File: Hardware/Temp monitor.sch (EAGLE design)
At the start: 41 parts, among them IC1 74LS595D, IC2 74LS595D, IC3 74LS595D, IC4 74LS595D, IC5 74LS595D, J2 TP_8, J3 USB-MICROB, T1 NPN, T2 NPN, T3 NPN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

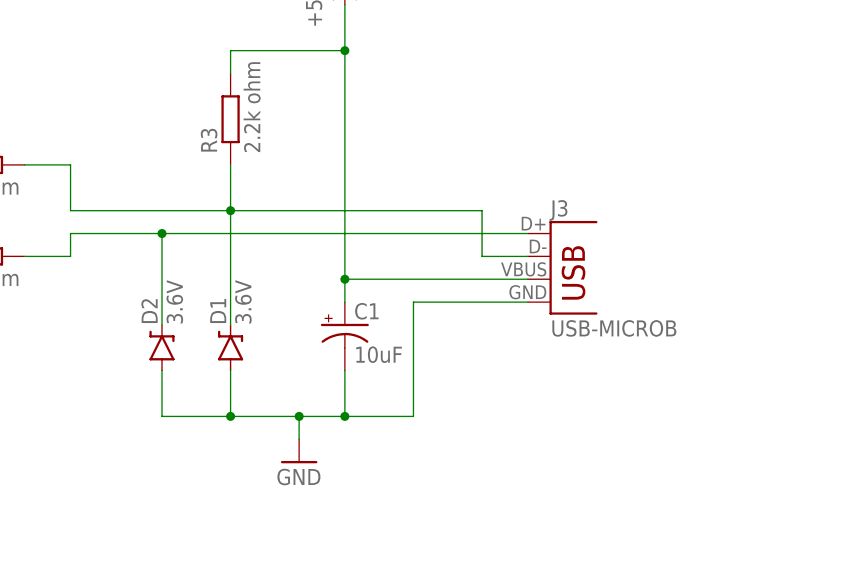
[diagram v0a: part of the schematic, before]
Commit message: Cleanup + through hole usb
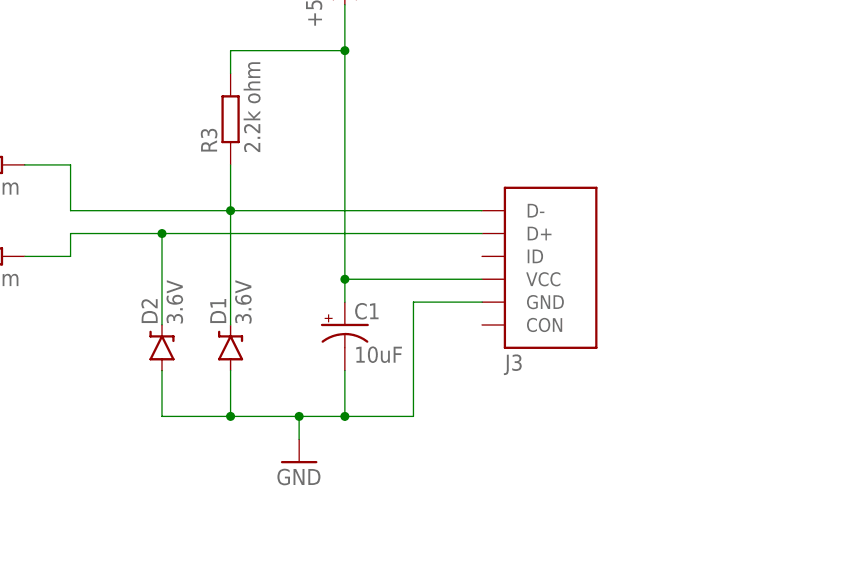
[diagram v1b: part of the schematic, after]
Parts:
- J3: value USB-MICROB -> ZX62D-B-5PA8; device SparkFun-Connectors:USB-MICROB -> usb:ZX62D-B-5PA8
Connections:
- net +5V: now also J3.VCC; no longer J3.VBUS
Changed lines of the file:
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@@
 <?xml version="1.0" encoding="utf-8"?>
 <!DOCTYPE eagle SYSTEM "eagle.dtd">
-<eagle version="7.7.0">
+<eagle version="8.0.2">
 <drawing>
 <settings>
@@
 <part name="R7" library="resistor" deviceset="R-EU_" device="R0805W" value="10k"/>
 <part name="P+13" library="supply1" deviceset="+5V" device=""/>
-<part name="J3" library="SparkFun-Connectors" deviceset="USB" device="-MICROB"/>
 <part name="U$1" library="TempMonitor" deviceset="LOGO" device=""/>
 <part name="U$2" library="TempMonitor" deviceset="LOGO" device=""/>
@@
 <part name="C6" library="resistor" deviceset="C-EU" device="C0805" value="0.1uF"/>
 <part name="FRAME1" library="frames" deviceset="A3L-LOC" device=""/>
+<part name="J3" library="usb" deviceset="ZX62D-B-5PA8" device=""/>
 </parts>
 <sheets>
@@
 <instance part="R7" gate="G$1" x="269.24" y="102.87" rot="R90"/>
 <instance part="P+13" gate="1" x="269.24" y="115.57"/>
-<instance part="J3" gate="G$1" x="353.06" y="78.74"/>
 <instance part="U$1" gate="G$1" x="290.83" y="7.62"/>
 <instance part="U$2" gate="G$1" x="290.83" y="7.62"/>
@@
 <instance part="C6" gate="G$1" x="203.2" y="86.36" rot="R180"/>
 <instance part="FRAME1" gate="G$1" x="0" y="0"/>
+<instance part="J3" gate="G$1" x="347.98" y="78.74"/>
 </instances>
 <busses>
@@
 <wire x1="317.5" y1="104.14" x2="317.5" y2="106.68" width="0.1524" layer="91"/>
 <wire x1="317.5" y1="106.68" x2="330.2" y2="106.68" width="0.1524" layer="91"/>
-<wire x1="330.2" y1="81.28" x2="330.2" y2="106.68" width="0.1524" layer="91"/>
+<wire x1="330.2" y1="78.74" x2="330.2" y2="81.28" width="0.1524" layer="91"/>
 <junction x="330.2" y="106.68"/>
 <pinref part="C1" gate="G$1" pin="+"/>
-<pinref part="J3" gate="G$1" pin="VBUS"/>
-<wire x1="330.2" y1="81.28" x2="330.2" y2="78.74" width="0.1524" layer="91"/>
-<wire x1="350.52" y1="81.28" x2="330.2" y2="81.28" width="0.1524" layer="91"/>
+<pinref part="J3" gate="G$1" pin="VCC"/>
+<wire x1="330.2" y1="81.28" x2="330.2" y2="106.68" width="0.1524" layer="91"/>
+<wire x1="345.44" y1="81.28" x2="330.2" y2="81.28" width="0.1524" layer="91"/>
 <junction x="330.2" y="81.28"/>
 </segment>
@@
 <wire x1="337.82" y1="66.04" x2="330.2" y2="66.04" width="0.1524" layer="91"/>
 <junction x="330.2" y="66.04"/>
+<wire x1="337.82" y1="78.74" x2="337.82" y2="66.04" width="0.1524" layer="91"/>
 <pinref part="J3" gate="G$1" pin="GND"/>
-<wire x1="350.52" y1="78.74" x2="337.82" y2="78.74" width="0.1524" layer="91"/>
-<wire x1="337.82" y1="78.74" x2="337.82" y2="66.04" width="0.1524" layer="91"/>
+<wire x1="345.44" y1="78.74" x2="337.82" y2="78.74" width="0.1524" layer="91"/>
 </segment>
 <segment>
@@
 <wire x1="317.5" y1="76.2" x2="317.5" y2="88.9" width="0.1524" layer="91"/>
 <junction x="317.5" y="88.9"/>
-<pinref part="J3" gate="G$1" pin="D-"/>
-<wire x1="350.52" y1="83.82" x2="345.44" y2="83.82" width="0.1524" layer="91"/>
-<wire x1="345.44" y1="83.82" x2="345.44" y2="88.9" width="0.1524" layer="91"/>
 <pinref part="R3" gate="G$1" pin="1"/>
 <wire x1="317.5" y1="93.98" x2="317.5" y2="88.9" width="0.1524" layer="91"/>
+<pinref part="J3" gate="G$1" pin="D-"/>
 </segment>
 </net>
 <net name="N$2" class="0">
 <segment>
-<wire x1="350.52" y1="86.36" x2="309.88" y2="86.36" width="0.1524" layer="91"/>
 <wire x1="309.88" y1="86.36" x2="299.72" y2="86.36" width="0.1524" layer="91"/>
 <wire x1="299.72" y1="86.36" x2="299.72" y2="83.82" width="0.1524" layer="91"/>
@@
 <pinref part="D2" gate="G$1" pin="C"/>
 <wire x1="309.88" y1="76.2" x2="309.88" y2="86.36" width="0.1524" layer="91"/>
+<pinref part="J3" gate="G$1" pin="D+"/>
+<wire x1="309.88" y1="86.36" x2="345.44" y2="86.36" width="0.1524" layer="91"/>
 <junction x="309.88" y="86.36"/>
-<pinref part="J3" gate="G$1" pin="D+"/>
 </segment>
 </net>
